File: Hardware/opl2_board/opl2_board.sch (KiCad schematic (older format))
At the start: 24 parts, among them J1 Conn_01x40

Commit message: opl2 board progress
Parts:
- removed U? (x7): 74LS04, Package_DIP:DIP-14_W7.62mm_Socket, symbol 74xx:74LS04
- removed U?: 74LS04, Package_DIP:DIP-14_W7.62mm_Socket, symbol adlib:YM3014B
- removed U? (x3): 74LS04, Package_DIP:DIP-14_W7.62mm_Socket, symbol Amplifier_Operational:LM358
- added D2: LED, LED_SMD:LED_1206_3216Metric_Pad1.42x1.75mm_HandSolder, symbol Device:LED
- added R2: 330R, Resistor_SMD:R_0805_2012Metric_Pad1.15x1.40mm_HandSolder, symbol Device:R_Small
- added U1: 74HC00, Package_DIP:DIP-14_W7.62mm_Socket, symbol 74xx:74HC00
- added U3: YM3014B, Package_DIP:DIP-8_W7.62mm_Socket, symbol adlib:YM3014B
- added U4: LM358, Package_DIP:DIP-8_W7.62mm_Socket, symbol Amplifier_Operational:LM358
- C4, C5: renamed from C?; footprint Capacitor_THT:C_Disc_D3.8mm_W2.6mm_P2.50mm -> Capacitor_SMD:C_1206_3216Metric_Pad1.42x1.75mm_HandSolder
- U2: renamed from U?; value 74LS04 -> YM3812; footprint Package_DIP:DIP-14_W7.62mm_Socket -> Package_DIP:DIP-24_W15.24mm_Socket
- gave numbers to parts that had none: 9
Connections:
- wire segments 87 -> 95

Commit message: Backplane provides diode and pullups for SLOW signal
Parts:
- removed D1: 1N4148, Diode_THT:D_DO-35_SOD27_P7.62mm_Horizontal, symbol pspice:DIODE
- removed R1: 1k, Resistor_SMD:R_0805_2012Metric_Pad1.15x1.40mm_HandSolder, symbol Device:R_Small
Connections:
- wire segments 95 -> 92
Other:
- note added: "Diode + pullup provided by backplane"
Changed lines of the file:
@@
 ~SLOW~
-$Comp
-L pspice:DIODE D1
-U 1 1 60349715
-P 3100 6150
-F 0 "D1" H 3100 5885 50  0000 C CNN
-F 1 "1N4148" H 3100 5976 50  0000 C CNN
-F 2 "Diode_THT:D_DO-35_SOD27_P7.62mm_Horizontal" H 3100 6150 50  0001 C CNN
-F 3 "~" H 3100 6150 50  0001 C CNN
-	1    3100 6150
-	-1   0    0    1
-$EndComp
-Wire Wire Line
-	3550 6150 3400 6150
-Wire Wire Line
-	2900 6150 2750 6150
-$Comp
-L Device:R_Small R1
-U 1 1 6035227C
-P 3400 5900
-F 0 "R1" H 3459 5946 50  0000 L CNN
-F 1 "1k" H 3459 5855 50  0000 L CNN
-F 2 "Resistor_SMD:R_0805_2012Metric_Pad1.15x1.40mm_HandSolder" H 3400 5900 50  0001 C CNN
-F 3 "~" H 3400 5900 50  0001 C CNN
-	1    3400 5900
-	1    0    0    -1
-$EndComp
-Wire Wire Line
-	3400 6000 3400 6150
-Connection ~ 3400 6150
-Wire Wire Line
-	3400 6150 3300 6150
-$Comp
-L power:+5V #PWR0120
-U 1 1 603555C6
-P 3400 5800
-F 0 "#PWR0120" H 3400 5650 50  0001 C CNN
-F 1 "+5V" H 3415 5973 50  0000 C CNN
-F 2 "" H 3400 5800 50  0001 C CNN
-F 3 "" H 3400 5800 50  0001 C CNN
-	1    3400 5800
-	1    0    0    -1
-$EndComp
 $Comp
 L 74xx:74HC00 U1
@@
 	1    0    0    -1
 $EndComp
+Wire Wire Line
+	3550 6150 2750 6150
+Text Notes 2400 6000 0    50   ~ 0
+Diode + pullup provided by backplane
 $EndSCHEMATC

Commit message: Through hole components for OPL2 board
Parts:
- C1, C2, C3, C6, C7: value C_Small -> 4.7u; footprint Capacitor_SMD:C_1206_3216Metric_Pad1.42x1.75mm_HandSolder -> Capacitor_THT:C_Disc_D4.3mm_W1.9mm_P5.00mm
- C4, C5: footprint Capacitor_SMD:C_1206_3216Metric_Pad1.42x1.75mm_HandSolder -> Capacitor_THT:C_Disc_D4.3mm_W1.9mm_P5.00mm
- D2: footprint LED_SMD:LED_1206_3216Metric_Pad1.42x1.75mm_HandSolder -> LED_THT:LED_D3.0mm_Horizontal_O3.81mm_Z6.0mm
- R2: footprint Resistor_SMD:R_0805_2012Metric_Pad1.15x1.40mm_HandSolder -> Resistor_THT:R_Axial_DIN0204_L3.6mm_D1.6mm_P5.08mm_Horizontal
- U2: symbol adlib:YM3812 -> opl2_board-rescue:YM3812-adlib
- U3: symbol adlib:YM3014B -> opl2_board-rescue:YM3014B-adlib
- X1: value CXO_DIP8 -> 3.579545 MHz
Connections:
- net labels added: GNDA
- wire segments 92 -> 90
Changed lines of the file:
@@
 Wire Wire Line
 	850  3600 1700 3600
-$Comp
-L adlib:YM3812 U2
-U 1 1 6033A272
-P 5250 3150
-F 0 "U2" H 5200 4163 60  0000 C CNN
-F 1 "YM3812" H 5200 4057 60  0000 C CNN
-F 2 "Package_DIP:DIP-24_W15.24mm_Socket" H 5250 3050 60  0000 C CNN
-F 3 "" H 5250 3150 60  0000 C CNN
-	1    5250 3150
-	1    0    0    -1
-$EndComp
 Text GLabel 4750 2450 0    50   BiDi ~ 0
 D0
@@
 P 10100 1000
 F 0 "C7" V 9871 1000 50  0000 C CNN
-F 1 "C_Small" V 9962 1000 50  0000 C CNN
-F 2 "Capacitor_SMD:C_1206_3216Metric_Pad1.42x1.75mm_HandSolder" H 10100 1000 50  0001 C CNN
+F 1 "4.7u" V 9962 1000 50  0000 C CNN
+F 2 "Capacitor_THT:C_Disc_D4.3mm_W1.9mm_P5.00mm" H 10100 1000 50  0001 C CNN
 F 3 "~" H 10100 1000 50  0001 C CNN
 	1    10100 1000
@@
 P 5600 1700
 F 0 "C2" V 5371 1700 50  0000 C CNN
-F 1 "C_Small" V 5462 1700 50  0000 C CNN
-F 2 "Capacitor_SMD:C_1206_3216Metric_Pad1.42x1.75mm_HandSolder" H 5600 1700 50  0001 C CNN
+F 1 "4.7u" V 5462 1700 50  0000 C CNN
+F 2 "Capacitor_THT:C_Disc_D4.3mm_W1.9mm_P5.00mm" H 5600 1700 50  0001 C CNN
 F 3 "~" H 5600 1700 50  0001 C CNN
 	1    5600 1700
@@
 	7550 2800 7800 2800
 $Comp
-L power:GND #PWR0111
+L power:GNDA #PWR0111
 U 1 1 603BB655
 P 7800 3300
 F 0 "#PWR0111" H 7800 3050 50  0001 C CNN
-F 1 "GND" H 7805 3127 50  0000 C CNN
+F 1 "GNDA" H 7805 3127 50  0000 C CNN
 F 2 "" H 7800 3300 50  0001 C CNN
 F 3 "" H 7800 3300 50  0001 C CNN
@@
 Wire Wire Line
 	7500 3450 7500 3300
-Wire Wire Line
-	7500 3300 7600 3300
 $Comp
 L Device:C C5
@@
 F 0 "C5" H 7315 2996 50  0000 L CNN
 F 1 "10uF" H 7315 2905 50  0000 L CNN
-F 2 "Capacitor_SMD:C_1206_3216Metric_Pad1.42x1.75mm_HandSolder" H 7238 2800 50  0001 C CNN
+F 2 "Capacitor_THT:C_Disc_D4.3mm_W1.9mm_P5.00mm" H 7238 2800 50  0001 C CNN
 F 3 "~" H 7200 2950 50  0001 C CNN
 	1    7200 2950
@@
 Wire Wire Line
 	7200 2800 7450 2800
-Wire Wire Line
-	7200 3100 7600 3100
-Wire Wire Line
-	7600 3100 7600 3300
-Connection ~ 7600 3300
-Wire Wire Line
-	7600 3300 7800 3300
 $Comp
 L Device:C C4
@@
 F 0 "C4" H 7015 3146 50  0000 L CNN
 F 1 "10uF" H 7015 3055 50  0000 L CNN
-F 2 "Capacitor_SMD:C_1206_3216Metric_Pad1.42x1.75mm_HandSolder" H 6938 2950 50  0001 C CNN
+F 2 "Capacitor_THT:C_Disc_D4.3mm_W1.9mm_P5.00mm" H 6938 2950 50  0001 C CNN
 F 3 "~" H 6900 3100 50  0001 C CNN
 	1    6900 3100
@@
 Wire Wire Line
 	7250 2700 7550 2700
-Wire Wire Line
-	6900 3250 7500 3250
-Wire Wire Line
-	7500 3250 7500 3300
-Connection ~ 7500 3300
 $Comp
 L power:GND #PWR0112
@@
 P 6900 1700
 F 0 "C3" V 6671 1700 50  0000 C CNN
-F 1 "C_Small" V 6762 1700 50  0000 C CNN
-F 2 "Capacitor_SMD:C_1206_3216Metric_Pad1.42x1.75mm_HandSolder" H 6900 1700 50  0001 C CNN
+F 1 "4.7u" V 6762 1700 50  0000 C CNN
+F 2 "Capacitor_THT:C_Disc_D4.3mm_W1.9mm_P5.00mm" H 6900 1700 50  0001 C CNN
 F 3 "~" H 6900 1700 50  0001 C CNN
 	1    6900 1700
@@
 P 3950 5050
 F 0 "X1" H 4294 5096 50  0000 L CNN
-F 1 "CXO_DIP8" H 4294 5005 50  0000 L CNN
+F 1 "3.579545 MHz" H 4294 5005 50  0000 L CNN
 F 2 "Oscillator:Oscillator_DIP-8" H 4400 4700 50  0001 C CNN
 F 3 "http://cdn-reichelt.de/documents/datenblatt/B400/OSZI.pdf" H 3850 5050 50  0001 C CNN
@@
 P 4300 4600
 F 0 "C1" V 4071 4600 50  0000 C CNN
-F 1 "C_Small" V 4162 4600 50  0000 C CNN
-F 2 "Capacitor_SMD:C_1206_3216Metric_Pad1.42x1.75mm_HandSolder" H 4300 4600 50  0001 C CNN
+F 1 "4.7u" V 4162 4600 50  0000 C CNN
+F 2 "Capacitor_THT:C_Disc_D4.3mm_W1.9mm_P5.00mm" H 4300 4600 50  0001 C CNN
 F 3 "~" H 4300 4600 50  0001 C CNN
 	1    4300 4600
@@
 P 9150 900
 F 0 "C6" V 8921 900 50  0000 C CNN
-F 1 "C_Small" V 9012 900 50  0000 C CNN
-F 2 "Capacitor_SMD:C_1206_3216Metric_Pad1.42x1.75mm_HandSolder" H 9150 900 50  0001 C CNN
+F 1 "4.7u" V 9012 900 50  0000 C CNN
+F 2 "Capacitor_THT:C_Disc_D4.3mm_W1.9mm_P5.00mm" H 9150 900 50  0001 C CNN
 F 3 "~" H 9150 900 50  0001 C CNN
 	1    9150 900
@@
 F 0 "D2" H 3843 1467 50  0000 C CNN
 F 1 "LED" H 3843 1376 50  0000 C CNN
-F 2 "LED_SMD:LED_1206_3216Metric_Pad1.42x1.75mm_HandSolder" H 3850 1250 50  0001 C CNN
+F 2 "LED_THT:LED_D3.0mm_Horizontal_O3.81mm_Z6.0mm" H 3850 1250 50  0001 C CNN
 F 3 "~" H 3850 1250 50  0001 C CNN
 	1    3850 1250
@@
 F 0 "R2" H 3409 1296 50  0000 L CNN
 F 1 "330R" H 3409 1205 50  0000 L CNN
-F 2 "Resistor_SMD:R_0805_2012Metric_Pad1.15x1.40mm_HandSolder" H 3350 1250 50  0001 C CNN
+F 2 "Resistor_THT:R_Axial_DIN0204_L3.6mm_D1.6mm_P5.08mm_Horizontal" H 3350 1250 50  0001 C CNN
 F 3 "~" H 3350 1250 50  0001 C CNN
 	1    3350 1250
@@
 	1    0    0    -1
 $EndComp
-$Comp
-L adlib:YM3014B U3
+Wire Wire Line
+	3550 6150 2750 6150
+Text Notes 2400 6000 0    50   ~ 0
+Diode + pullup provided by backplane
+$Comp
+L power:GND #PWR0120
+U 1 1 612E6AF8
+P 6950 4300
+F 0 "#PWR0120" H 6950 4050 50  0001 C CNN
+F 1 "GND" H 6955 4127 50  0000 C CNN
+F 2 "" H 6950 4300 50  0001 C CNN
+F 3 "" H 6950 4300 50  0001 C CNN
+	1    6950 4300
+	1    0    0    -1
+$EndComp
+$Comp
+L power:GNDA #PWR0124
+U 1 1 612E9200
+P 7350 4300
+F 0 "#PWR0124" H 7350 4050 50  0001 C CNN
+F 1 "GNDA" H 7355 4127 50  0000 C CNN
+F 2 "" H 7350 4300 50  0001 C CNN
+F 3 "" H 7350 4300 50  0001 C CNN
+	1    7350 4300
+	1    0    0    -1
+$EndComp
+Wire Wire Line
+	7500 3300 7800 3300
+Wire Wire Line
+	7200 3100 7200 3250
+Wire Wire Line
+	7200 3250 6900 3250
+$Comp
+L power:GND #PWR0125
+U 1 1 612FD955
+P 6900 3250
+F 0 "#PWR0125" H 6900 3000 50  0001 C CNN
+F 1 "GND" H 6905 3077 50  0000 C CNN
+F 2 "" H 6900 3250 50  0001 C CNN
+F 3 "" H 6900 3250 50  0001 C CNN
+	1    6900 3250
+	1    0    0    -1
+$EndComp
+$Comp
+L opl2_board-rescue:YM3014B-adlib U3
 U 1 1 604D5363
 P 6550 2550
@@
 	1    0    0    -1
 $EndComp
-Wire Wire Line
-	3550 6150 2750 6150
-Text Notes 2400 6000 0    50   ~ 0
-Diode + pullup provided by backplane
+$Comp
+L opl2_board-rescue:YM3812-adlib U2
+U 1 1 6033A272
+P 5250 3150
+F 0 "U2" H 5200 4163 60  0000 C CNN
+F 1 "YM3812" H 5200 4057 60  0000 C CNN
+F 2 "Package_DIP:DIP-24_W15.24mm_Socket" H 5250 3050 60  0000 C CNN
+F 3 "" H 5250 3150 60  0000 C CNN
+	1    5250 3150
+	1    0    0    -1
+$EndComp
+Wire Wire Line
+	7350 4300 6950 4300
 $EndSCHEMATC

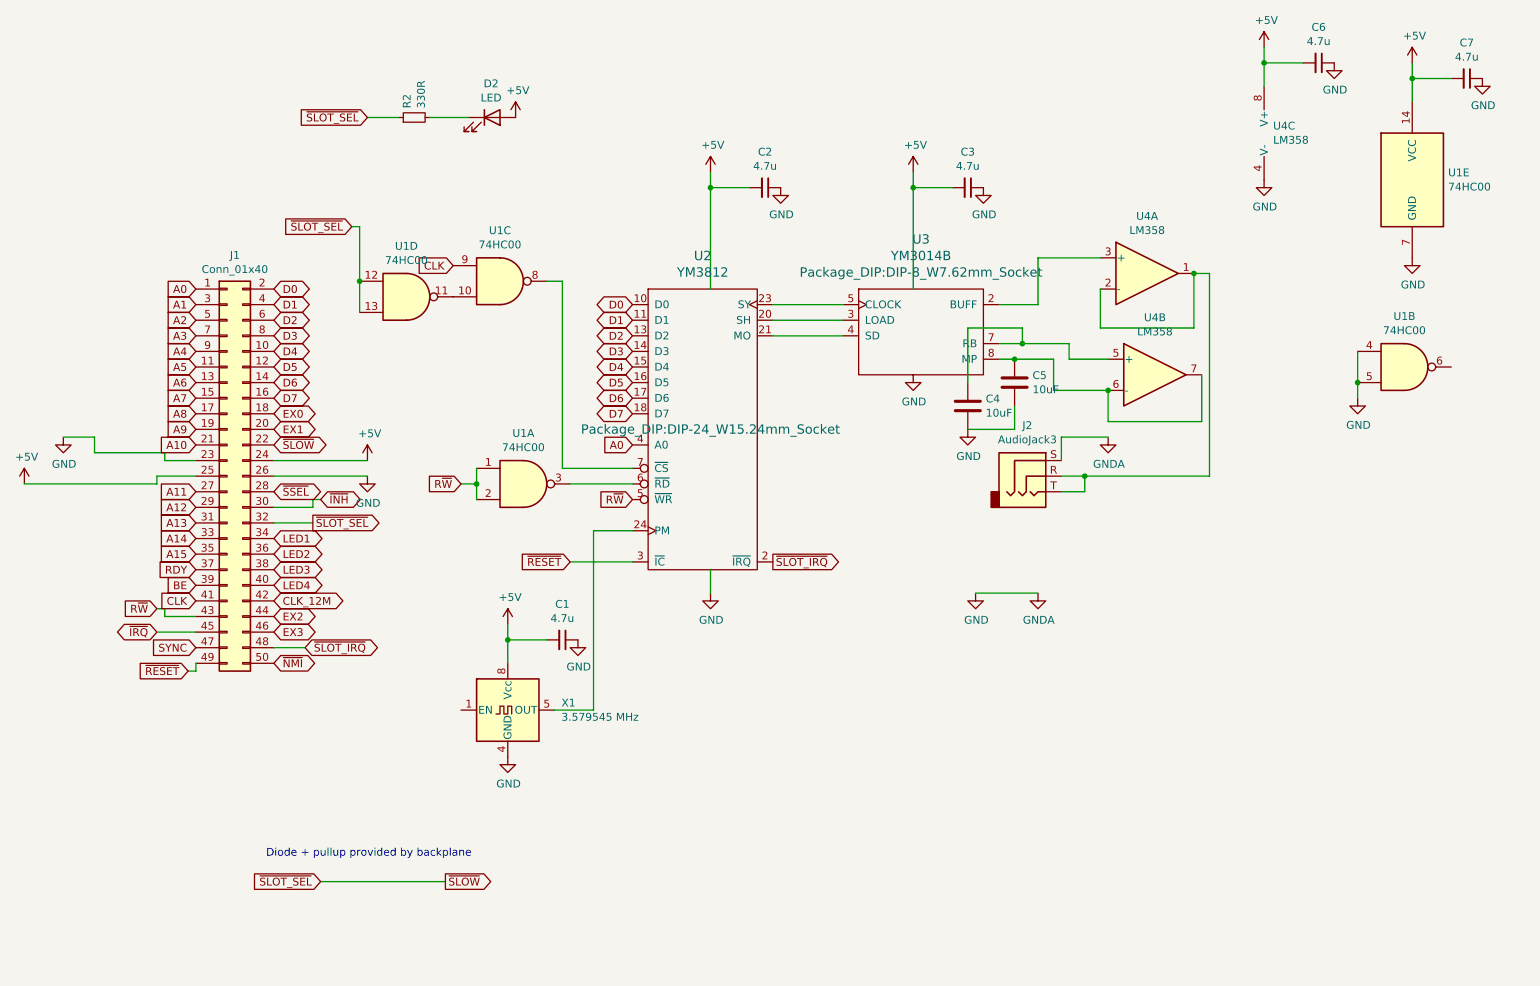
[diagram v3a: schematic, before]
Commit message: final update for through hole conversion
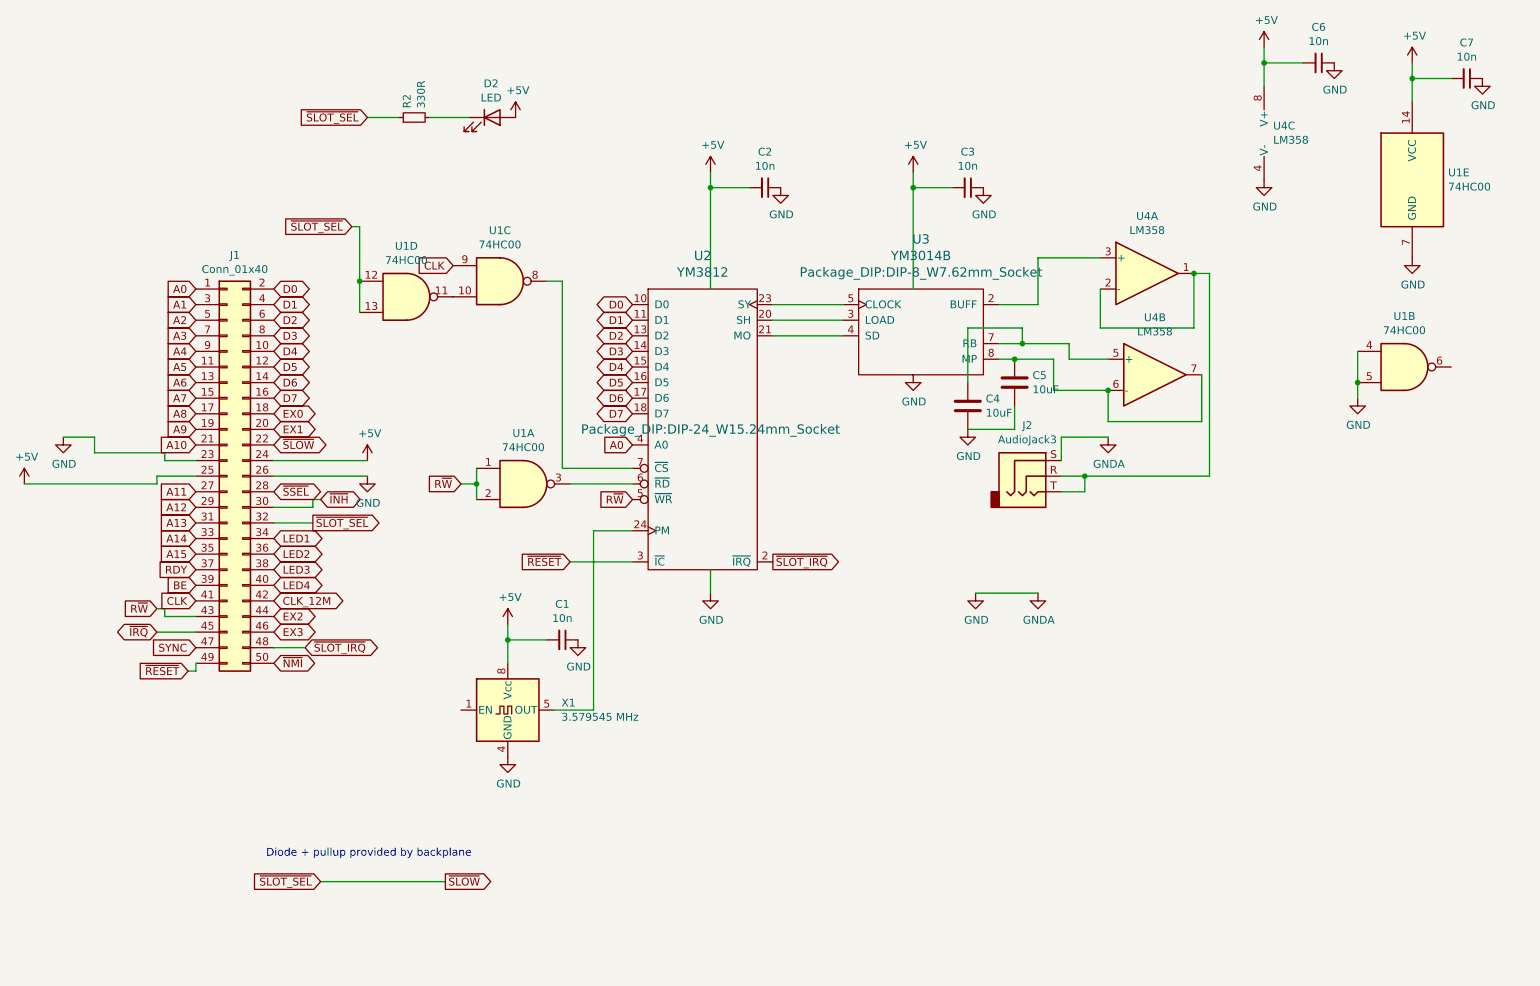
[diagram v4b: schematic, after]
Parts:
- C1, C2, C3, C6, C7: value 4.7u -> 10n
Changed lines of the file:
@@
 P 10100 1000
 F 0 "C7" V 9871 1000 50  0000 C CNN
-F 1 "4.7u" V 9962 1000 50  0000 C CNN
+F 1 "10n" V 9962 1000 50  0000 C CNN
 F 2 "Capacitor_THT:C_Disc_D4.3mm_W1.9mm_P5.00mm" H 10100 1000 50  0001 C CNN
 F 3 "~" H 10100 1000 50  0001 C CNN
@@
 P 5600 1700
 F 0 "C2" V 5371 1700 50  0000 C CNN
-F 1 "4.7u" V 5462 1700 50  0000 C CNN
+F 1 "10n" V 5462 1700 50  0000 C CNN
 F 2 "Capacitor_THT:C_Disc_D4.3mm_W1.9mm_P5.00mm" H 5600 1700 50  0001 C CNN
 F 3 "~" H 5600 1700 50  0001 C CNN
@@
 P 6900 1700
 F 0 "C3" V 6671 1700 50  0000 C CNN
-F 1 "4.7u" V 6762 1700 50  0000 C CNN
+F 1 "10n" V 6762 1700 50  0000 C CNN
 F 2 "Capacitor_THT:C_Disc_D4.3mm_W1.9mm_P5.00mm" H 6900 1700 50  0001 C CNN
 F 3 "~" H 6900 1700 50  0001 C CNN
@@
 P 4300 4600
 F 0 "C1" V 4071 4600 50  0000 C CNN
-F 1 "4.7u" V 4162 4600 50  0000 C CNN
+F 1 "10n" V 4162 4600 50  0000 C CNN
 F 2 "Capacitor_THT:C_Disc_D4.3mm_W1.9mm_P5.00mm" H 4300 4600 50  0001 C CNN
 F 3 "~" H 4300 4600 50  0001 C CNN
@@
 P 9150 900
 F 0 "C6" V 8921 900 50  0000 C CNN
-F 1 "4.7u" V 9012 900 50  0000 C CNN
+F 1 "10n" V 9012 900 50  0000 C CNN
 F 2 "Capacitor_THT:C_Disc_D4.3mm_W1.9mm_P5.00mm" H 9150 900 50  0001 C CNN
 F 3 "~" H 9150 900 50  0001 C CNN

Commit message: bigger resistors on OPL2 board
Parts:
- R2: footprint Resistor_THT:R_Axial_DIN0204_L3.6mm_D1.6mm_P5.08mm_Horizontal -> Resistor_THT:R_Axial_DIN0207_L6.3mm_D2.5mm_P10.16mm_Horizontal
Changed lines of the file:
@@
 F 0 "R2" H 3409 1296 50  0000 L CNN
 F 1 "330R" H 3409 1205 50  0000 L CNN
-F 2 "Resistor_THT:R_Axial_DIN0204_L3.6mm_D1.6mm_P5.08mm_Horizontal" H 3350 1250 50  0001 C CNN
+F 2 "Resistor_THT:R_Axial_DIN0207_L6.3mm_D2.5mm_P10.16mm_Horizontal" H 3350 1250 50  0001 C CNN
 F 3 "~" H 3350 1250 50  0001 C CNN
 	1    3350 1250
@@
 Wire Wire Line
 	3700 1250 3450 1250
-Wire Wire Line
-	3250 1250 3050 1250
 $Comp
 L Amplifier_Operational:LM358 U4
@@
 Wire Wire Line
 	7350 4300 6950 4300
+Wire Wire Line
+	3050 1250 3250 1250
 $EndSCHEMATC

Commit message: change audio jack footprint
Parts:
- J2: value AudioJack3 -> AudioJack; footprint Connector_Audio:Jack_3.5mm_CUI_SJ1-3533NG_Horizontal -> Connector_Audio:Jack_3.5mm_PJ320E_Horizontal; symbol Connector:AudioJack3 -> Connector:AudioJack4
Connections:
- net GND: now also J2.R2
- net at J2.T, U4.1, U4.2 (-): now also J2.R1; no longer J2.R
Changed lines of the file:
@@
 $EndComp
 Wire Wire Line
-	7500 3550 7650 3550
+	7500 3650 7650 3650
 Wire Wire Line
 	8450 3550 8450 2250
@@
 	8450 2250 8350 2250
 Wire Wire Line
-	7500 3650 7650 3650
+	7500 3750 7650 3750
 Wire Wire Line
 	7650 3650 7650 3550
-Connection ~ 7650 3550
 Wire Wire Line
 	7650 3550 8450 3550
 $Comp
-L Connector:AudioJack3 J2
+L Connector:AudioJack4 J2
 U 1 1 603BB663
 P 7300 3550
 F 0 "J2" H 7282 3875 50  0000 C CNN
-F 1 "AudioJack3" H 7282 3784 50  0000 C CNN
-F 2 "Connector_Audio:Jack_3.5mm_CUI_SJ1-3533NG_Horizontal" H 7300 3550 50  0001 C CNN
+F 1 "AudioJack" H 7282 3784 50  0000 C CNN
+F 2 "Connector_Audio:Jack_3.5mm_PJ320E_Horizontal" H 7300 3550 50  0001 C CNN
 F 3 "~" H 7300 3550 50  0001 C CNN
 	1    7300 3550
@@
 Wire Wire Line
 	3050 1250 3250 1250
+Wire Wire Line
+	7650 3650 7650 3750
+Connection ~ 7650 3650
+Wire Wire Line
+	7500 3550 7500 3450
+Connection ~ 7500 3450
 $EndSCHEMATC

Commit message: update gerbers
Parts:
- removed D2: LED, LED_THT:LED_D3.0mm_Horizontal_O3.81mm_Z6.0mm, symbol Device:LED
- removed R2: 330R, Resistor_THT:R_Axial_DIN0207_L6.3mm_D2.5mm_P10.16mm_Horizontal, symbol Device:R_Small
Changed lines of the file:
@@
 Connection ~ 3000 2300
-$Comp
-L Device:LED D2
-U 1 1 6049AA52
-P 3850 1250
-F 0 "D2" H 3843 1467 50  0000 C CNN
-F 1 "LED" H 3843 1376 50  0000 C CNN
-F 2 "LED_THT:LED_D3.0mm_Horizontal_O3.81mm_Z6.0mm" H 3850 1250 50  0001 C CNN
-F 3 "~" H 3850 1250 50  0001 C CNN
-	1    3850 1250
-	1    0    0    -1
-$EndComp
-Text GLabel 3050 1250 0    50   Input ~ 0
-~SLOT_SEL~
-$Comp
-L power:+5V #PWR0123
-U 1 1 6049D7AB
-P 4000 1250
-F 0 "#PWR0123" H 4000 1100 50  0001 C CNN
-F 1 "+5V" H 4015 1423 50  0000 C CNN
-F 2 "" H 4000 1250 50  0001 C CNN
-F 3 "" H 4000 1250 50  0001 C CNN
-	1    4000 1250
-	1    0    0    -1
-$EndComp
-$Comp
-L Device:R_Small R2
-U 1 1 604ABF00
-P 3350 1250
-F 0 "R2" H 3409 1296 50  0000 L CNN
-F 1 "330R" H 3409 1205 50  0000 L CNN
-F 2 "Resistor_THT:R_Axial_DIN0207_L6.3mm_D2.5mm_P10.16mm_Horizontal" H 3350 1250 50  0001 C CNN
-F 3 "~" H 3350 1250 50  0001 C CNN
-	1    3350 1250
-	0    -1   -1   0
-$EndComp
-Wire Wire Line
-	3700 1250 3450 1250
 $Comp
 L Amplifier_Operational:LM358 U4
@@
 	7350 4300 6950 4300
 Wire Wire Line
-	3050 1250 3250 1250
-Wire Wire Line
 	7650 3650 7650 3750
